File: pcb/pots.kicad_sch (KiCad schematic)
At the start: 9 parts, among them SW1 SW_DIP_x03

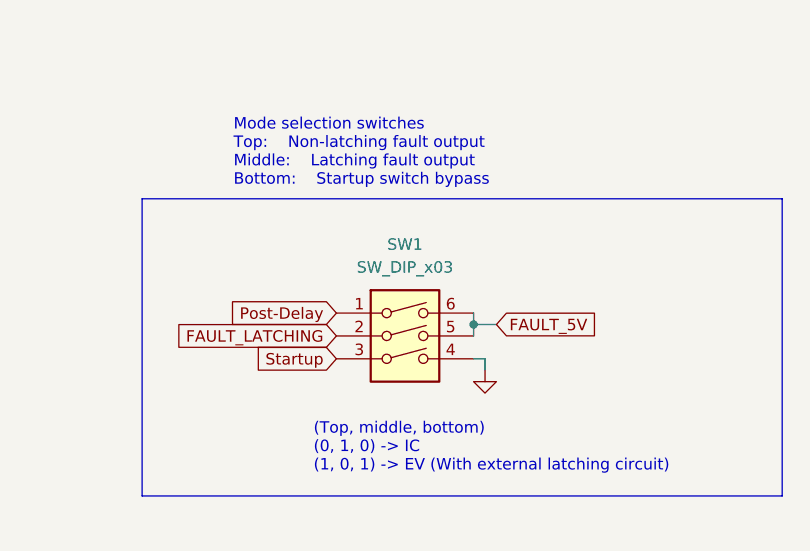
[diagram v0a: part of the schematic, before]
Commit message: Added jlc part number for dip switches
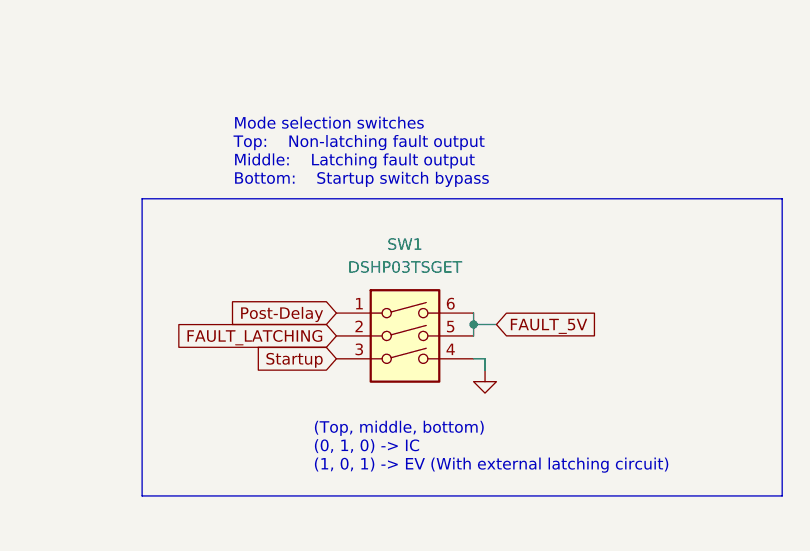
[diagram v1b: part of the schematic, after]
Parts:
- SW1: value SW_DIP_x03 -> DSHP03TSGET; LCSC DSHP03TSGET -> C50844
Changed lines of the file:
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@@
     (in_bom yes) (on_board yes) (fields_autoplaced)
     (property "Reference" "SW1" (id 0) (at 193.04 86.36 0))
-    (property "Value" "SW_DIP_x03" (id 1) (at 193.04 88.9 0))
+    (property "Value" "DSHP03TSGET" (id 1) (at 193.04 88.9 0))
     (property "Footprint" "Button_Switch_SMD:SW_DIP_SPSTx03_Slide_KingTek_DSHP03TS_W7.62mm_P1.27mm" (id 2) (at 193.04 99.06 0)
       (effects (font (size 1.27 1.27)) hide)
@@
       (effects (font (size 1.27 1.27)) hide)
     )
-    (property "LCSC" "DSHP03TSGET" (id 4) (at 193.04 99.06 0)
+    (property "LCSC" "C50844" (id 4) (at 193.04 99.06 0)
       (effects (font (size 1.27 1.27)) hide)
     )

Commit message: Update to KiCad 7, bump project revision/date
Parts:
- RV1, RV2, RV3, RV4, RV5, RV6, RV7, RV8: Spice_Lib_File SPICE models/pot.lib -> (none); Spice_Model Potentiometer -> (none); Spice_Netlist_Enabled Y -> (none); Spice_Primitive X -> (none)
